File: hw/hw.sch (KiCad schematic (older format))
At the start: 14 parts, among them U1 74LS299, U2 74LS138, U3 Z80CPU, U4 74LS161, U5 CY7C199, U6 74LS107, X1 CXO_DIP8

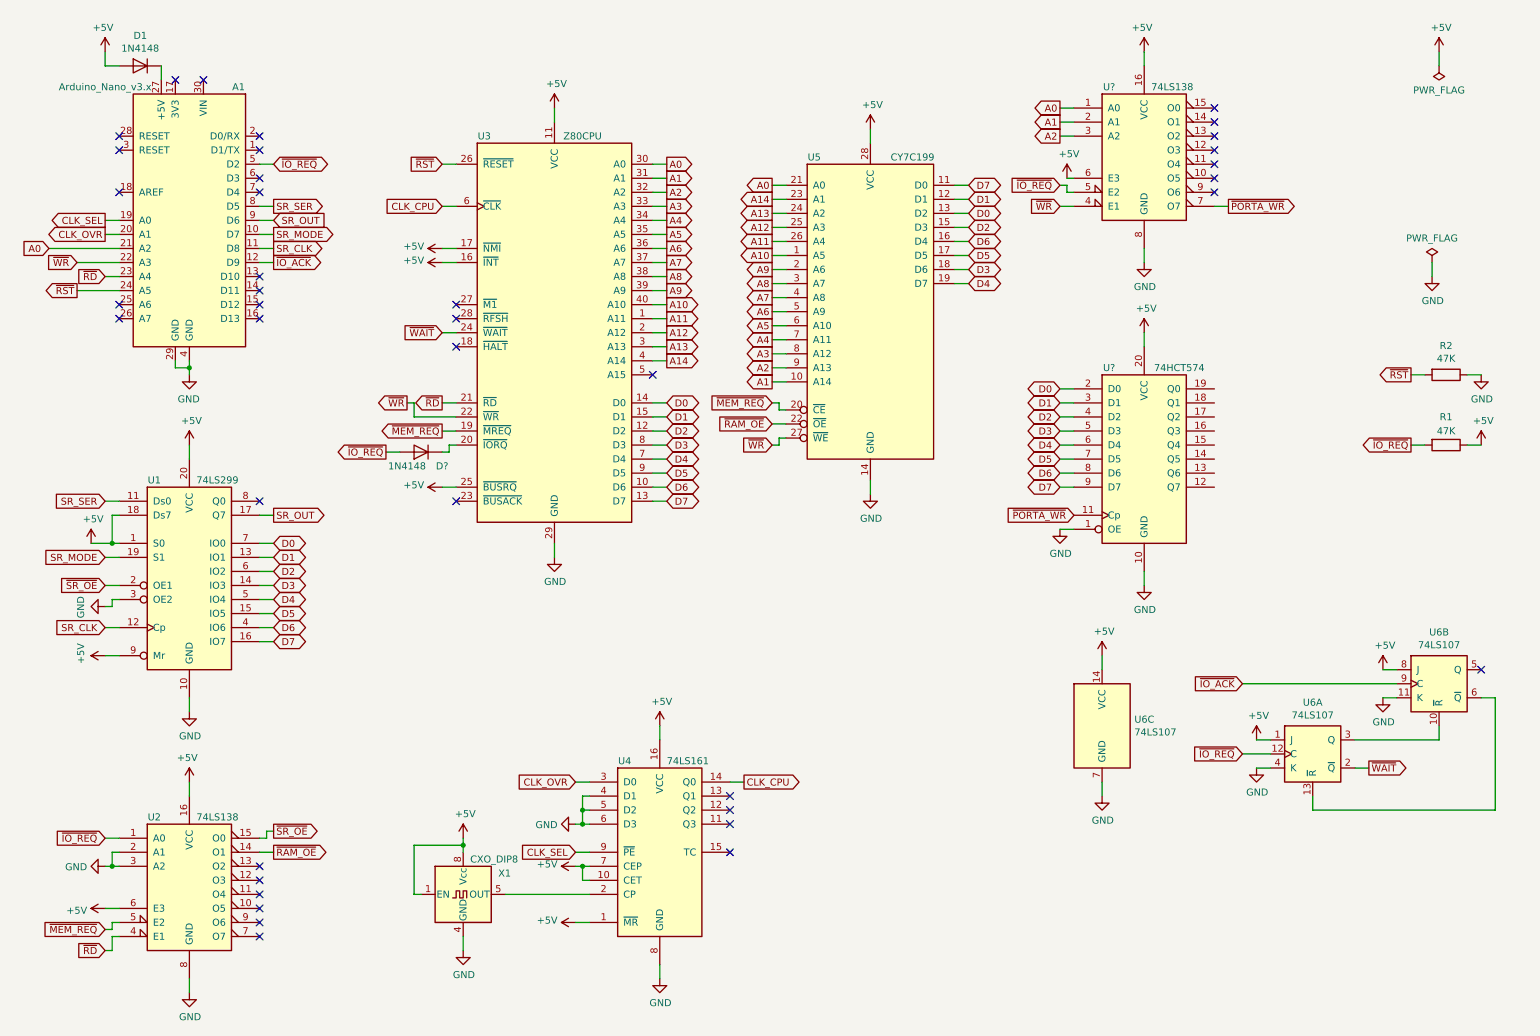
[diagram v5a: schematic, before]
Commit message: partially isolate Arduino port
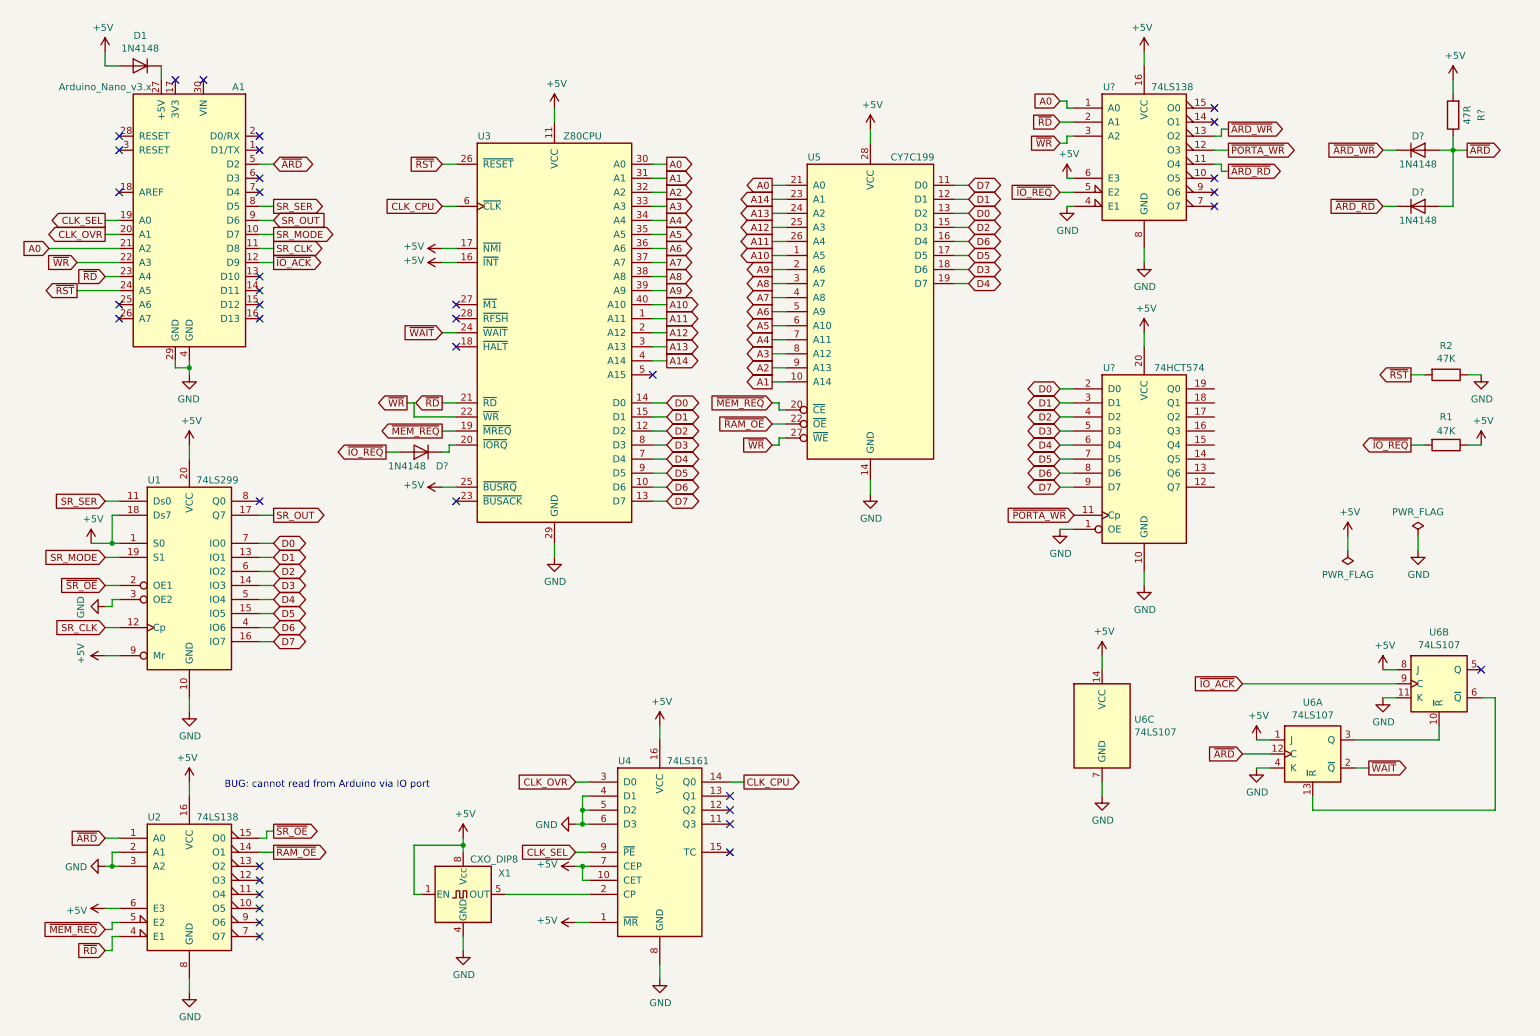
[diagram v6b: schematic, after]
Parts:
- added D? (x2): 1N4148, Diode_THT:D_DO-35_SOD27_P7.62mm_Horizontal, symbol Diode:1N4148
- added R?: 47R, symbol Device:R
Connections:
- net +5V: now also R?.2
- net A1: no longer U?.2 (A1)
- net A2: no longer U?.3 (A2)
- net GND: now also U?.4 (E1)
- net ~IO_REQ: no longer A1.5 (D2), U2.1 (A0), U6.12 (C)
- net ~PORTA_WR: now also U?.12 (O3); no longer U?.7 (O7)
- net ~RD: now also U?.2 (A1)
- net ~WR: now also U?.3 (A2); no longer U?.4 (E1)
- net ~ARD_RD: now reaches U?.11 (O4)
- net ~ARD_RD: now also D?.1 (K)
- net ~ARD_WR: now reaches U?.13 (O2)
- net ~ARD_WR: now also D?.1 (K)
- new net ~ARD: A1.5 (D2), D?.2 (A), D?.2 (A), R?.1, U2.1 (A0), U6.12 (C)
- no-connect marks 39 -> 37
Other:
- note added: "BUG: cannot read from Arduino via IO port"
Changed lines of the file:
@@
 L power:+5V #PWR0125
 U 1 1 5D457D7E
-P 10600 800
-F 0 "#PWR0125" H 10600 650 50  0001 C CNN
-F 1 "+5V" H 10615 973 50  0000 C CNN
-F 2 "" H 10600 800 50  0001 C CNN
-F 3 "" H 10600 800 50  0001 C CNN
-	1    10600 800
+P 9950 4250
+F 0 "#PWR0125" H 9950 4100 50  0001 C CNN
+F 1 "+5V" H 9965 4423 50  0000 C CNN
+F 2 "" H 9950 4250 50  0001 C CNN
+F 3 "" H 9950 4250 50  0001 C CNN
+	1    9950 4250
 	1    0    0    -1
 $EndComp
@@
 L power:PWR_FLAG #FLG0101
 U 1 1 5D457DDB
-P 10600 900
-F 0 "#FLG0101" H 10600 975 50  0001 C CNN
-F 1 "PWR_FLAG" H 10600 1073 50  0000 C CNN
-F 2 "" H 10600 900 50  0001 C CNN
-F 3 "~" H 10600 900 50  0001 C CNN
-	1    10600 900
+P 9950 4350
+F 0 "#FLG0101" H 9950 4425 50  0001 C CNN
+F 1 "PWR_FLAG" H 9950 4523 50  0000 C CNN
+F 2 "" H 9950 4350 50  0001 C CNN
+F 3 "~" H 9950 4350 50  0001 C CNN
+	1    9950 4350
 	-1   0    0    1
 $EndComp
 Wire Wire Line
-	10600 900  10600 800
+	9950 4350 9950 4250
 NoConn ~ 5000 3100
 Wire Wire Line
@@
 L power:PWR_FLAG #FLG01
 U 1 1 5D4751A2
-P 10550 2300
-F 0 "#FLG01" H 10550 2375 50  0001 C CNN
-F 1 "PWR_FLAG" H 10550 2473 50  0000 C CNN
-F 2 "" H 10550 2300 50  0001 C CNN
-F 3 "~" H 10550 2300 50  0001 C CNN
-	1    10550 2300
-	1    0    0    -1
-$EndComp
-Wire Wire Line
-	10550 2300 10550 2400
+P 10450 4250
+F 0 "#FLG01" H 10450 4325 50  0001 C CNN
+F 1 "PWR_FLAG" H 10450 4423 50  0000 C CNN
+F 2 "" H 10450 4250 50  0001 C CNN
+F 3 "~" H 10450 4250 50  0001 C CNN
+	1    10450 4250
+	1    0    0    -1
+$EndComp
+Wire Wire Line
+	10450 4250 10450 4350
 $Comp
 L power:GND #PWR012
 U 1 1 5D489F33
-P 10550 2400
-F 0 "#PWR012" H 10550 2150 50  0001 C CNN
-F 1 "GND" H 10555 2227 50  0000 C CNN
-F 2 "" H 10550 2400 50  0001 C CNN
-F 3 "" H 10550 2400 50  0001 C CNN
-	1    10550 2400
+P 10450 4350
+F 0 "#PWR012" H 10450 4100 50  0001 C CNN
+F 1 "GND" H 10455 4177 50  0000 C CNN
+F 2 "" H 10450 4350 50  0001 C CNN
+F 3 "" H 10450 4350 50  0001 C CNN
+	1    10450 4350
 	1    0    0    -1
 $EndComp
@@
 	3550 3650 3500 3650
 Text GLabel 9200 5800 0    50   Input ~ 0
-~IO_REQ
+~ARD
 Text GLabel 3500 2800 0    50   Input ~ 0
 ~WAIT
@@
 NoConn ~ 2200 1700
 Text GLabel 2300 1600 2    50   BiDi ~ 0
-~IO_REQ
+~ARD
 Wire Wire Line
 	2300 1600 2200 1600
@@
 	3100 3650 3200 3650
 Text GLabel 1100 6400 0    50   Input ~ 0
-~IO_REQ
+~ARD
 Text GLabel 10400 3600 0    50   Output ~ 0
 ~IO_REQ
@@
 Wire Wire Line
 	8500 2800 8500 2900
-Text GLabel 7900 1200 0    50   Output ~ 0
+Text GLabel 7900 1150 0    50   Input ~ 0
 A0
 Wire Wire Line
-	8000 1200 7900 1200
-Text GLabel 7900 1300 0    50   Output ~ 0
-A1
-Text GLabel 7900 1400 0    50   Output ~ 0
-A2
-Wire Wire Line
 	7900 1300 8000 1300
-Wire Wire Line
-	8000 1400 7900 1400
 Text GLabel 7900 3200 0    50   BiDi ~ 0
 D0
@@
 Text GLabel 8000 4100 0    50   Input ~ 0
 ~PORTA_WR
-Text GLabel 9100 1900 2    50   Output ~ 0
+Text GLabel 9100 1500 2    50   Output ~ 0
 ~PORTA_WR
 Wire Wire Line
-	9000 1900 9100 1900
+	9000 1500 9100 1500
 NoConn ~ 9000 1800
-NoConn ~ 9000 1700
-NoConn ~ 9000 1600
-NoConn ~ 9000 1500
-NoConn ~ 9000 1400
 NoConn ~ 9000 1300
-Text GLabel 7900 1750 0    50   Input ~ 0
+Text GLabel 7900 1800 0    50   Input ~ 0
 ~IO_REQ
-Text GLabel 7900 1900 0    50   Input ~ 0
+Text GLabel 7900 1450 0    50   Input ~ 0
 ~WR
 Wire Wire Line
-	7900 1900 8000 1900
-Wire Wire Line
-	7900 1750 7950 1750
-Wire Wire Line
-	7950 1750 7950 1800
-Wire Wire Line
-	7950 1800 8000 1800
+	7950 1900 8000 1900
 $Comp
 L power:+5V #PWR?
@@
 Wire Wire Line
 	7950 1700 8000 1700
+$Comp
+L Diode:1N4148 D?
+U 1 1 5D43E501
+P 10450 1900
+F 0 "D?" H 10450 2000 50  0000 C CNN
+F 1 "1N4148" H 10450 1800 50  0000 C CNN
+F 2 "Diode_THT:D_DO-35_SOD27_P7.62mm_Horizontal" H 10450 1725 50  0001 C CNN
+F 3 "http://www.nxp.com/documents/data_sheet/1N4148_1N4448.pdf" H 10450 1900 50  0001 C CNN
+	1    10450 1900
+	1    0    0    -1
+$EndComp
+$Comp
+L Diode:1N4148 D?
+U 1 1 5D43E63D
+P 10450 1500
+F 0 "D?" H 10450 1600 50  0000 C CNN
+F 1 "1N4148" H 10450 1400 50  0000 C CNN
+F 2 "Diode_THT:D_DO-35_SOD27_P7.62mm_Horizontal" H 10450 1325 50  0001 C CNN
+F 3 "http://www.nxp.com/documents/data_sheet/1N4148_1N4448.pdf" H 10450 1500 50  0001 C CNN
+	1    10450 1500
+	1    0    0    -1
+$EndComp
+Wire Wire Line
+	10200 1900 10300 1900
+Wire Wire Line
+	10300 1500 10200 1500
+Wire Wire Line
+	10600 1500 10700 1500
+Wire Wire Line
+	10700 1500 10700 1900
+Wire Wire Line
+	10700 1900 10600 1900
+$Comp
+L power:+5V #PWR?
+U 1 1 5D465E59
+P 10700 1000
+F 0 "#PWR?" H 10700 850 50  0001 C CNN
+F 1 "+5V" H 10715 1173 50  0000 C CNN
+F 2 "" H 10700 1000 50  0001 C CNN
+F 3 "" H 10700 1000 50  0001 C CNN
+	1    10700 1000
+	1    0    0    -1
+$EndComp
+Wire Wire Line
+	10700 1400 10700 1500
+Connection ~ 10700 1500
+Wire Wire Line
+	7900 1800 8000 1800
+Text GLabel 7900 1300 0    50   Input ~ 0
+~RD
+Wire Wire Line
+	7900 1150 7950 1150
+Wire Wire Line
+	7950 1150 7950 1200
+Wire Wire Line
+	7950 1200 8000 1200
+Wire Wire Line
+	7900 1450 7950 1450
+Wire Wire Line
+	7950 1450 7950 1400
+Wire Wire Line
+	7950 1400 8000 1400
+$Comp
+L power:GND #PWR?
+U 1 1 5D4D1639
+P 7950 1900
+F 0 "#PWR?" H 7950 1650 50  0001 C CNN
+F 1 "GND" H 7955 1727 50  0000 C CNN
+F 2 "" H 7950 1900 50  0001 C CNN
+F 3 "" H 7950 1900 50  0001 C CNN
+	1    7950 1900
+	1    0    0    -1
+$EndComp
+Text GLabel 9100 1350 2    50   Output ~ 0
+~ARD_WR
+Wire Wire Line
+	9100 1350 9050 1350
+Wire Wire Line
+	9050 1350 9050 1400
+Wire Wire Line
+	9050 1400 9000 1400
+Text GLabel 9100 1650 2    50   Output ~ 0
+~ARD_RD
+Wire Wire Line
+	9000 1600 9050 1600
+Wire Wire Line
+	9050 1600 9050 1650
+Wire Wire Line
+	9050 1650 9100 1650
 NoConn ~ 9000 1200
+NoConn ~ 9000 1700
+NoConn ~ 9000 1900
+Text GLabel 10200 1500 0    50   Input ~ 0
+~ARD_WR
+Text GLabel 10200 1900 0    50   Input ~ 0
+~ARD_RD
+Text GLabel 10800 1500 2    50   Output ~ 0
+~ARD
+Wire Wire Line
+	10700 1500 10800 1500
+$Comp
+L Device:R R?
+U 1 1 5D5C2001
+P 10700 1250
+F 0 "R?" V 10500 1250 50  0000 C CNN
+F 1 "47R" V 10600 1250 50  0000 C CNN
+F 2 "" V 10630 1250 50  0001 C CNN
+F 3 "~" H 10700 1250 50  0001 C CNN
+	1    10700 1250
+	-1   0    0    1
+$EndComp
+Wire Wire Line
+	10700 1000 10700 1100
+Text Notes 1950 6050 0    50   ~ 0
+BUG: cannot read from Arduino via IO port
 $EndSCHEMATC

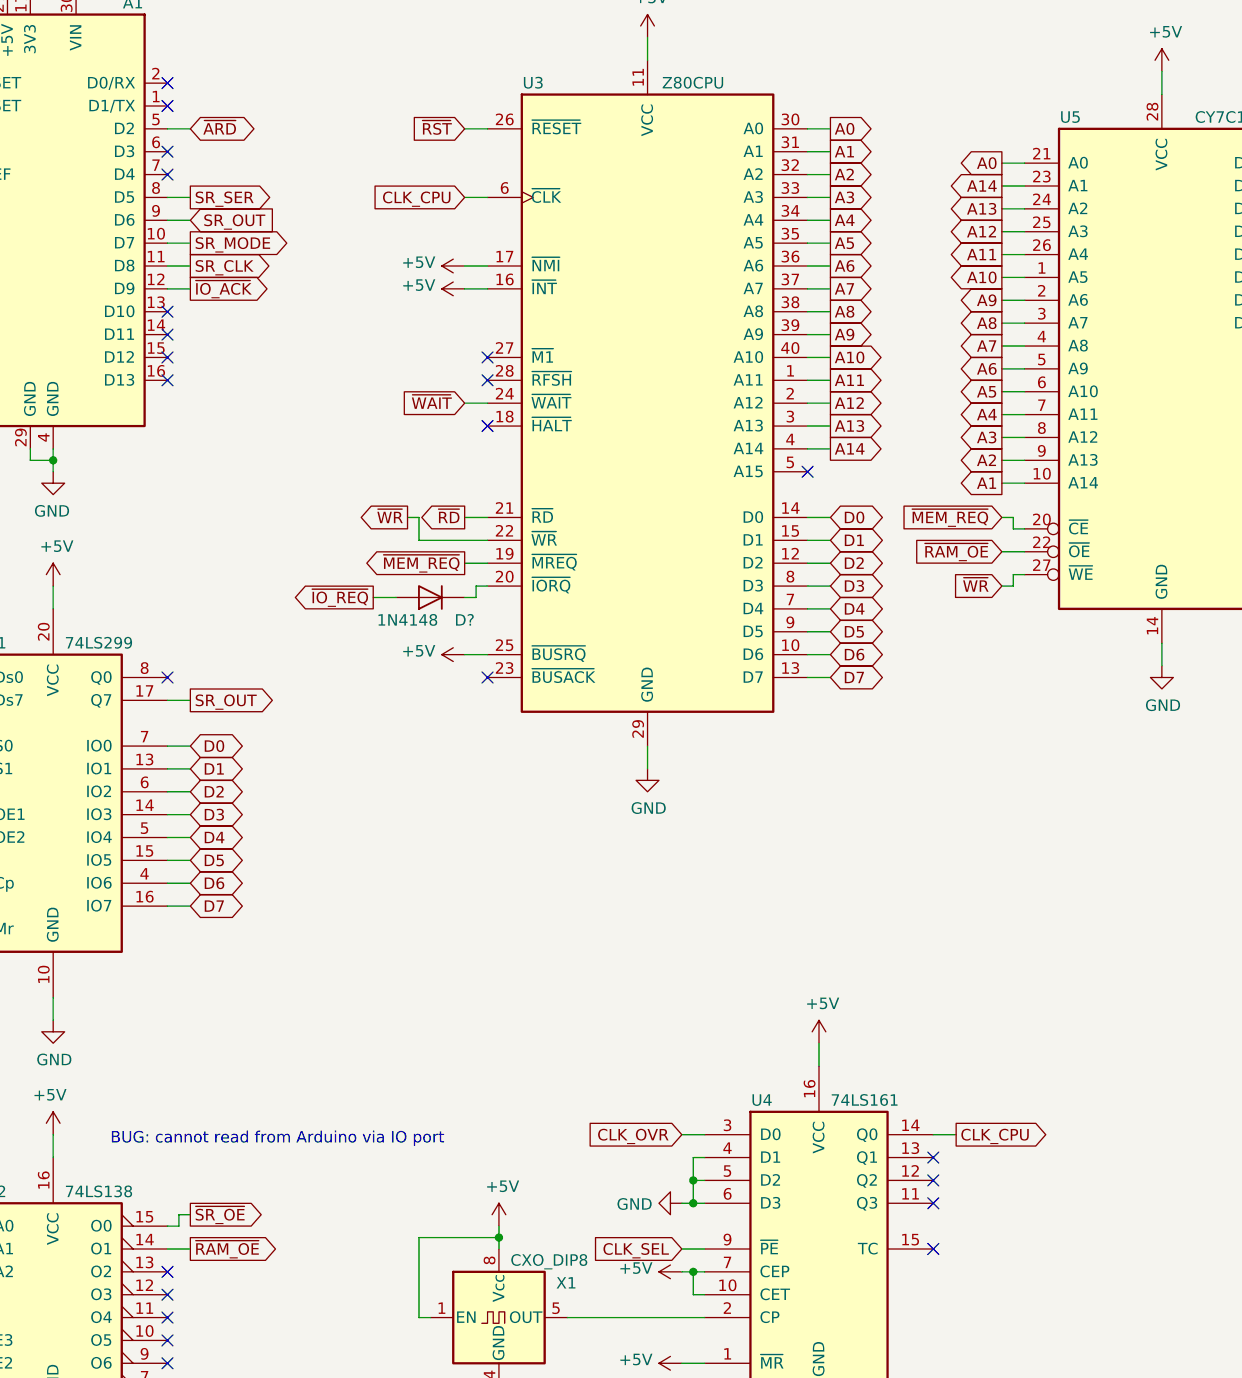
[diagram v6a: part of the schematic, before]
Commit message: add HSYNC and VSYNC signals
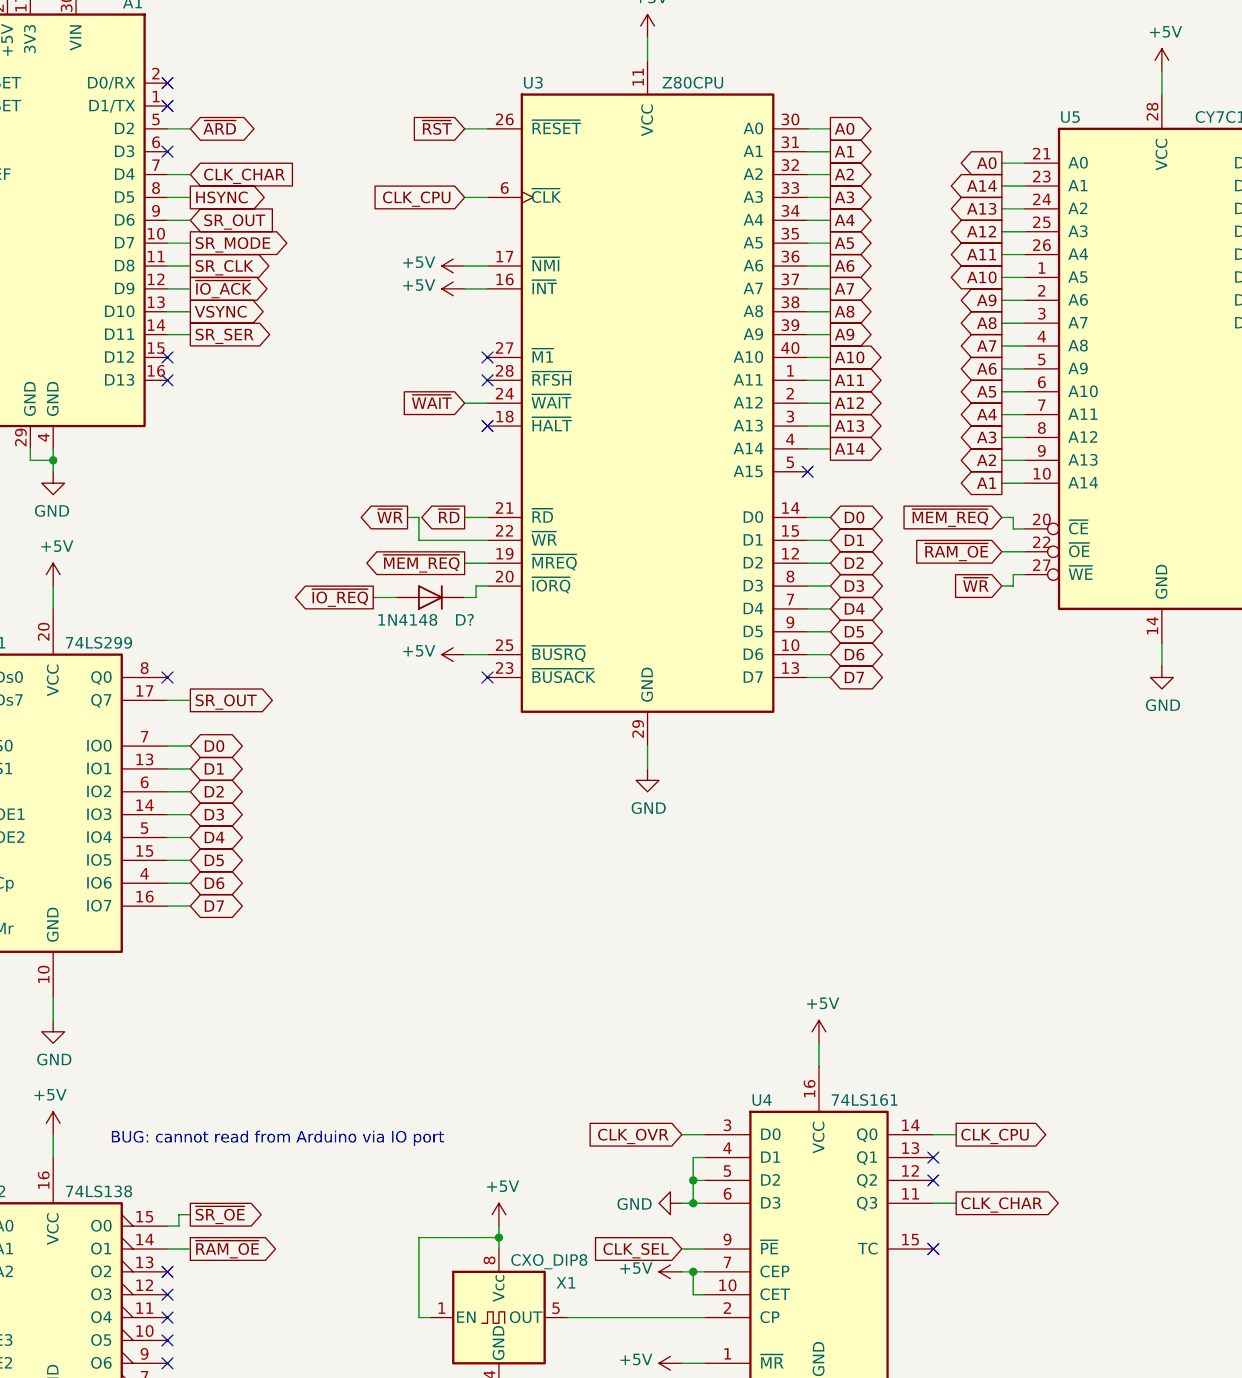
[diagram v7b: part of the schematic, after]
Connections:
- net SR_SER: now also A1.14 (D11); no longer A1.8 (D5)
- net CLK_CHAR: now reaches U4.11 (Q3)
- net CLK_CHAR: now also A1.7 (D4)
- net VSYNC: now reaches A1.13 (D10)
- new net HSYNC: A1.8 (D5)
- no-connect marks 37 -> 33
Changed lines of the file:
@@
 	4500 6200 4500 6300
 NoConn ~ 5550 6500
-NoConn ~ 5550 6300
 NoConn ~ 5550 6200
 NoConn ~ 5550 6100
@@
 Wire Wire Line
 	2250 6350 2300 6350
-Text GLabel 2300 1900 2    50   Output ~ 0
+Text GLabel 2300 2500 2    50   Output ~ 0
 SR_SER
 Text GLabel 2300 2100 2    50   Output ~ 0
@@
 	2200 2200 2300 2200
 Wire Wire Line
-	2200 1900 2300 1900
-NoConn ~ 2200 2400
-NoConn ~ 2200 2500
+	2200 2500 2300 2500
 NoConn ~ 2200 2600
 NoConn ~ 2200 2700
@@
 	-1   0    0    1
 $EndComp
-NoConn ~ 2200 1800
 Text GLabel 900  2300 0    50   Input ~ 0
 ~WR
@@
 Text Notes 1950 6050 0    50   ~ 0
 BUG: cannot read from Arduino via IO port
+Text GLabel 5650 6300 2    50   Output ~ 0
+CLK_CHAR
+Wire Wire Line
+	5650 6300 5550 6300
+Text GLabel 2300 1800 2    50   Input ~ 0
+CLK_CHAR
+Wire Wire Line
+	2200 1800 2300 1800
+Text GLabel 2300 1900 2    50   Output ~ 0
+HSYNC
+Wire Wire Line
+	2200 1900 2300 1900
+Text GLabel 2300 2400 2    50   Output ~ 0
+VSYNC
+Wire Wire Line
+	2300 2400 2200 2400
 $EndSCHEMATC
